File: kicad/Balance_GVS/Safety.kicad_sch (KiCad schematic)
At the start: 19 parts, among them K1 AQY210S, Q1 NPN, Q2 NPN, SW1 SW_Push, U4 INA303A1IPW, U6 OPA313IDCKR

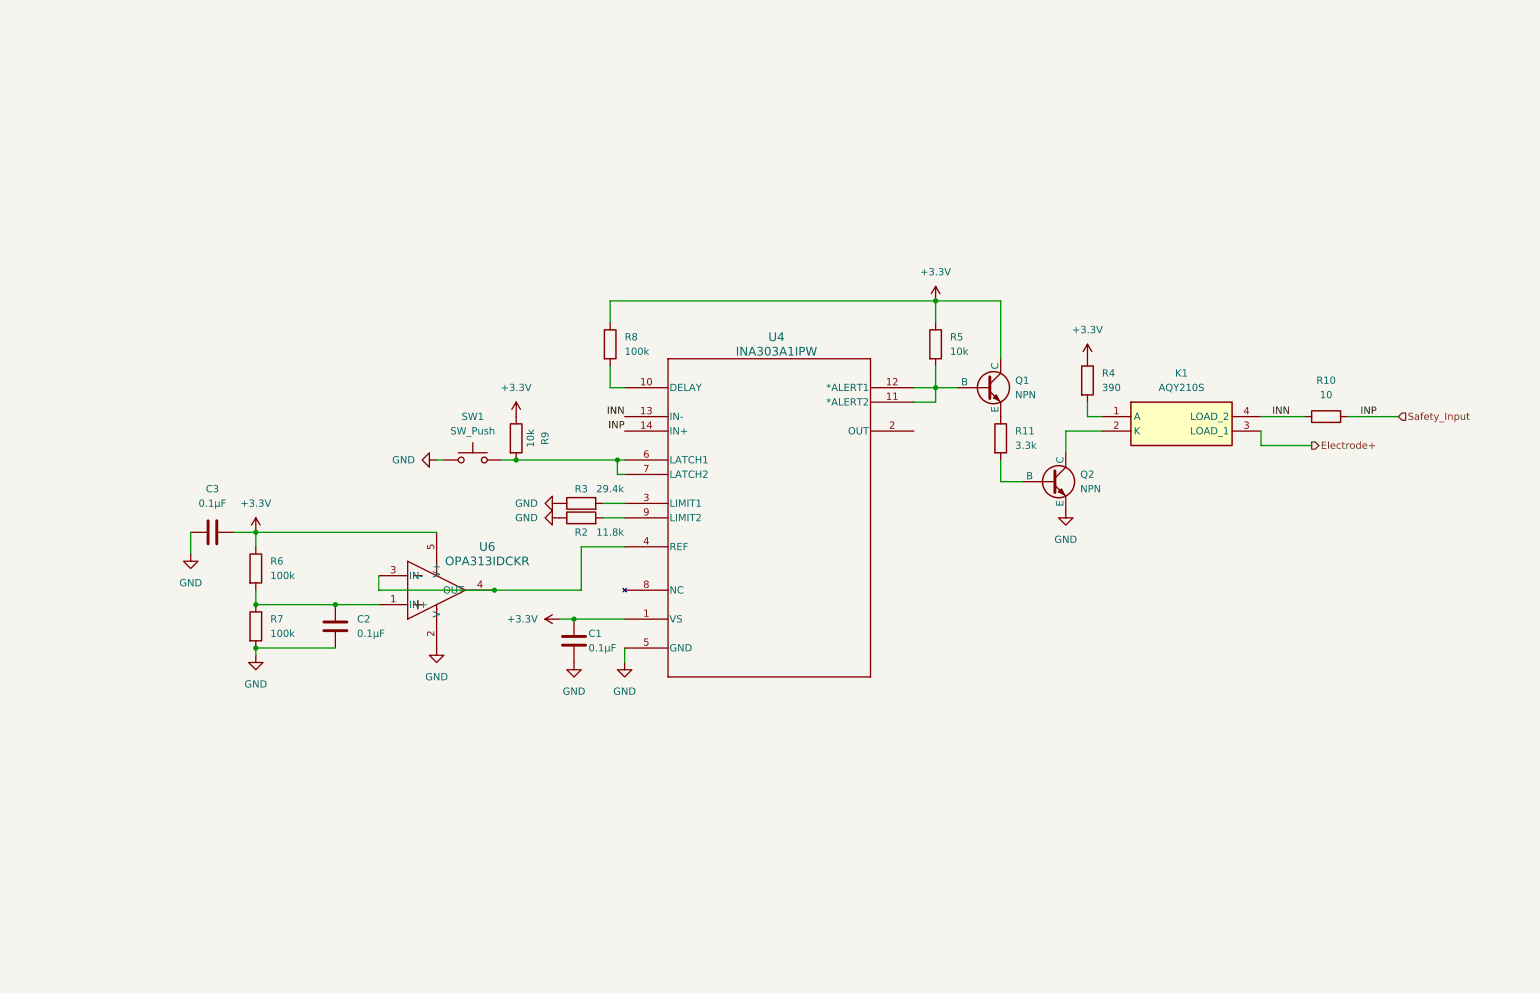
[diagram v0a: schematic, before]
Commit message: Update safety schematic with new limit set method
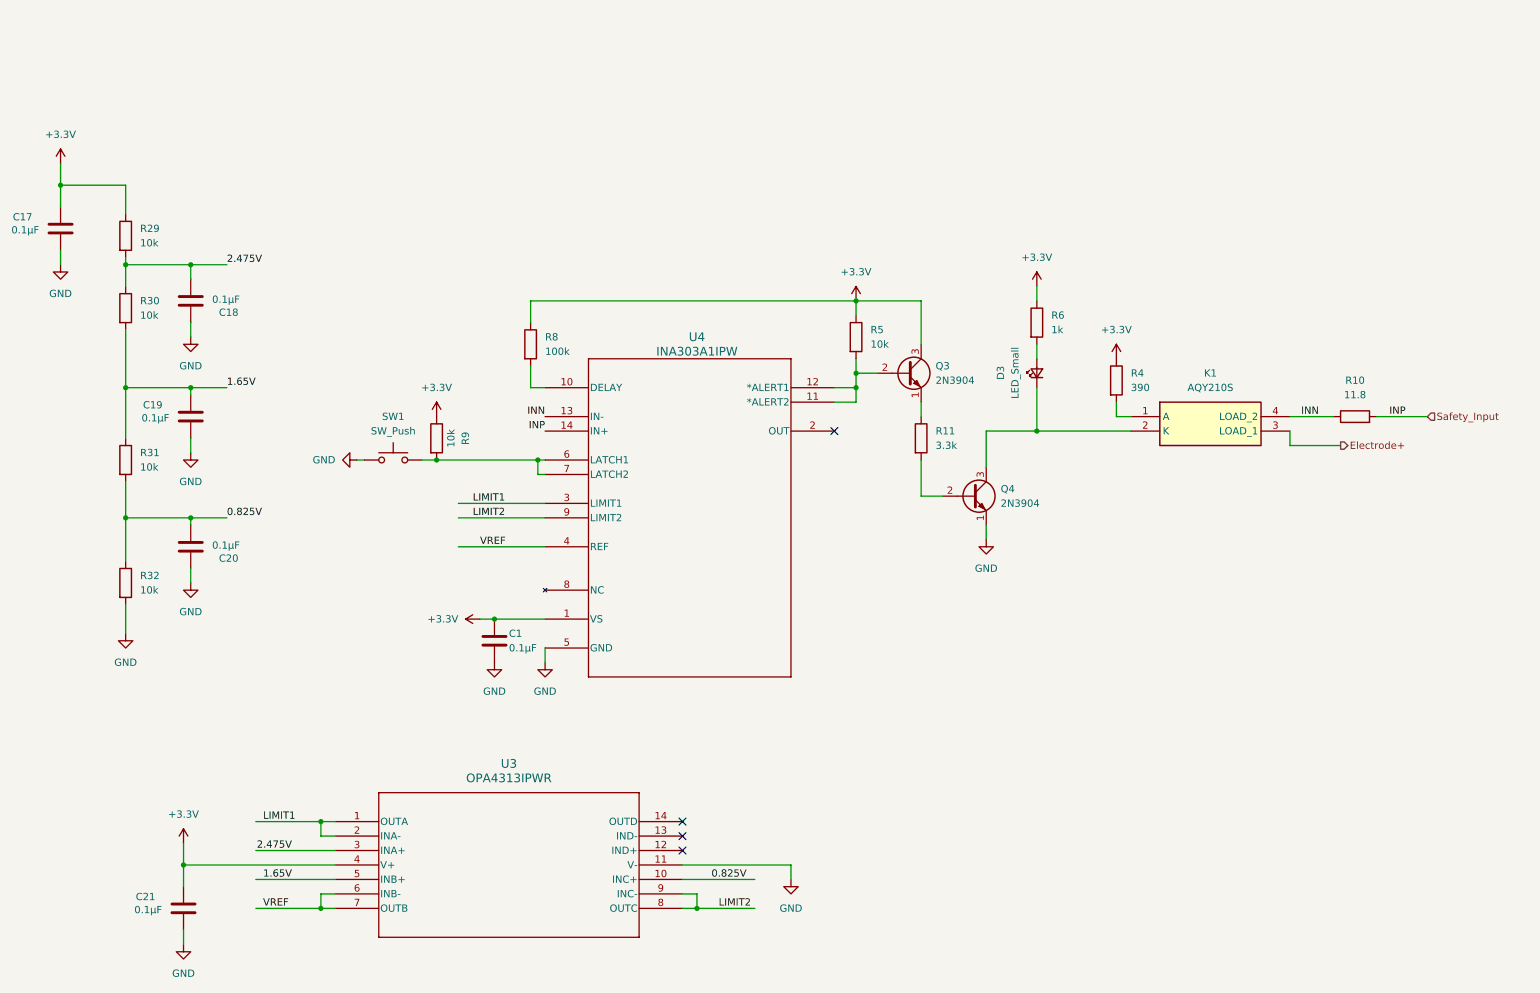
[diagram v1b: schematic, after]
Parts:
- removed C2, C3: 0.1µF, symbol Device:C
- removed Q1, Q2: NPN, symbol Simulation_SPICE:NPN
- removed R2: 11.8k, symbol Device:R
- removed R3: 29.4k, symbol Device:R
- removed R7: 100k, symbol Device:R
- removed U6: OPA313IDCKR, OPA313IDCKR_footprints:DCK0005A_N, symbol OPA313IDCKR:OPA313IDCKR
- added C17, C18, C19, C20, C21: 0.1µF, symbol Device:C
- added D3: LED_Small, symbol Device:LED_Small
- added Q3, Q4: 2N3904, Package_TO_SOT_THT:TO-92_Inline, symbol Transistor_BJT:2N3904
- added R29, R30, R31, R32: 10k, symbol Device:R
- added U3: OPA4313IPWR, PW14_TEX, symbol OPA4313IPWR:OPA4313IPWR
- R10: value 10 -> 11.8
- R6: value 100k -> 1k
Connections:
- net +3.3V: now also C17.1, C21.1, Q3.3 (C), R29.1, U3.4 (V+)
- net GND: now also C17.2, C18.1, C19.2, C20.1, C21.2, Q4.1 (E), R32.2, U3.11 (V-)
- net LIMIT1: now reaches U4.3 (LIMIT1)
- net LIMIT1: now also U3.1 (OUTA), U3.2 (INA-)
- net at R5.2, U4.11 (*ALERT2), U4.12 (*ALERT1): now also Q3.2 (B)
- net at R11.1: now also Q3.1 (E)
- net at K1.2 (K): now also D3.1 (K), Q4.3 (C)
- net LIMIT2: now reaches U4.9 (LIMIT2)
- net LIMIT2: now also U3.8 (OUTC), U3.9 (INC-)
- net at R6.2: now also D3.2 (A)
- net VREF: now reaches U4.4 (REF)
- net VREF: now also U3.6 (INB-), U3.7 (OUTB)
- net at R11.2: now also Q4.2 (B)
- new net 0.825V: C20.2, R31.2, R32.1, U3.10 (INC+)
- new net 1.65V: C19.1, R30.2, R31.1, U3.5 (INB+)
- new net 2.475V: C18.2, R29.2, R30.1, U3.3 (INA+)
- no-connect marks 0 -> 4
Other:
- moved on the sheet: C1, K1, R10, R11, R4, R5, R8, R9, SW1, U4

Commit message: Started adding howland connections
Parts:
- U3: footprint PW14_TEX -> OPA4313IPWR_footprints:PW14_TEX
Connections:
- net Electrode+ is gone; now on net INN: K1.3 (LOAD_1)
- net INN: no longer K1.4 (LOAD_2)
- net Safety_Input renamed Safety-
- new net Safety+: K1.4 (LOAD_2)
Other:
- moved on the sheet: R10
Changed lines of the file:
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@@
 	(wire
 		(pts
-			(xy 237.49 86.36) (xy 245.11 86.36)
+			(xy 248.92 86.36) (xy 248.92 85.09)
+		)
+		(stroke
+			(width 0)
+			(type default)
+		)
+	)
+	(wire
+		(pts
+			(xy 238.76 90.17) (xy 246.38 90.17)
 		)
 		(stroke
@@
 	(wire
 		(pts
+			(xy 237.49 86.36) (xy 248.92 86.36)
+		)
+		(stroke
+			(width 0)
+			(type default)
+		)
+	)
+	(wire
+		(pts
 			(xy 193.04 88.9) (xy 209.55 88.9)
 		)
@@
 	(wire
 		(pts
+			(xy 237.49 88.9) (xy 238.76 88.9)
+		)
+		(stroke
+			(width 0)
+			(type default)
+		)
+	)
+	(wire
+		(pts
 			(xy 106.68 129.54) (xy 106.68 127)
 		)
@@
 	(wire
 		(pts
-			(xy 252.73 86.36) (xy 261.62 86.36)
+			(xy 254 90.17) (xy 262.89 90.17)
 		)
 		(stroke
@@
 	(wire
 		(pts
-			(xy 55.88 162.56) (xy 69.85 162.56)
+			(xy 238.76 88.9) (xy 238.76 90.17)
 		)
 		(stroke
@@
 	(wire
 		(pts
-			(xy 104.14 66.04) (xy 161.29 66.04)
+			(xy 55.88 162.56) (xy 69.85 162.56)
 		)
 		(stroke
@@
 	(wire
 		(pts
-			(xy 184.15 88.9) (xy 193.04 88.9)
+			(xy 104.14 66.04) (xy 161.29 66.04)
 		)
 		(stroke
@@
 	(wire
 		(pts
-			(xy 44.45 59.69) (xy 50.8 59.69)
+			(xy 184.15 88.9) (xy 193.04 88.9)
 		)
 		(stroke
@@
 	(wire
 		(pts
-			(xy 172.72 66.04) (xy 172.72 73.66)
+			(xy 44.45 59.69) (xy 50.8 59.69)
 		)
 		(stroke
@@
 	(wire
 		(pts
-			(xy 85.09 93.98) (xy 87.63 93.98)
+			(xy 172.72 66.04) (xy 172.72 73.66)
 		)
 		(stroke
@@
 	(wire
 		(pts
-			(xy 33.02 59.69) (xy 44.45 59.69)
+			(xy 85.09 93.98) (xy 87.63 93.98)
 		)
 		(stroke
@@
 	(wire
 		(pts
-			(xy 33.02 97.79) (xy 33.02 111.76)
+			(xy 33.02 59.69) (xy 44.45 59.69)
 		)
 		(stroke
@@
 	(wire
 		(pts
-			(xy 237.49 88.9) (xy 237.49 91.44)
+			(xy 33.02 97.79) (xy 33.02 111.76)
 		)
 		(stroke
@@
 	(wire
 		(pts
-			(xy 237.49 91.44) (xy 246.38 91.44)
-		)
-		(stroke
-			(width 0)
-			(type default)
-		)
-	)
-	(wire
-		(pts
 			(xy 207.01 86.36) (xy 207.01 83.82)
 		)
@@
 	)
 	(label "INP"
-		(at 257.81 86.36 180)
+		(at 259.08 90.17 180)
 		(effects
 			(font
@@
 		)
 	)
-	(label "1.65V"
-		(at 62.23 167.64 180)
-		(effects
-			(font
-				(size 1.27 1.27)
-			)
-			(justify right bottom)
-		)
-	)
 	(label "LIMIT2"
 		(at 137.16 172.72 0)
@@
 	)
 	(label "INN"
-		(at 242.57 86.36 180)
+		(at 243.84 90.17 180)
 		(effects
 			(font
@@
 		)
 	)
-	(label "1.65V"
-		(at 50.8 81.28 0)
+	(global_label "1.65V"
+		(shape input)
+		(at 55.88 167.64 180)
+		(fields_autoplaced yes)
 		(effects
 			(font
 				(size 1.27 1.27)
 			)
-			(justify left bottom)
+			(justify right)
+		)
+		(property "Intersheetrefs" "${INTERSHEET_REFS}"
+			(at 47.5729 167.64 0)
+			(hide yes)
+			(show_name no)
+			(do_not_autoplace no)
+			(effects
+				(font
+					(size 1.27 1.27)
+				)
+				(justify right)
+			)
 		)
 	)
-	(hierarchical_label "Electrode+"
-		(shape output)
-		(at 246.38 91.44 0)
+	(global_label "Safety-"
+		(shape bidirectional)
+		(at 262.89 90.17 0)
+		(fields_autoplaced yes)
 		(effects
 			(font
@@
 			(justify left)
 		)
+		(property "Intersheetrefs" "${INTERSHEET_REFS}"
+			(at 274.425 90.17 0)
+			(hide yes)
+			(show_name no)
+			(do_not_autoplace no)
+			(effects
+				(font
+					(size 1.27 1.27)
+				)
+				(justify left)
+			)
+		)
 	)
-	(hierarchical_label "Safety_Input"
-		(shape input)
-		(at 261.62 86.36 0)
+	(global_label "Safety+"
+		(shape bidirectional)
+		(at 248.92 85.09 0)
+		(fields_autoplaced yes)
 		(effects
 			(font
@@
 			(justify left)
 		)
+		(property "Intersheetrefs" "${INTERSHEET_REFS}"
+			(at 260.455 85.09 0)
+			(hide yes)
+			(show_name no)
+			(do_not_autoplace no)
+			(effects
+				(font
+					(size 1.27 1.27)
+				)
+				(justify left)
+			)
+		)
+	)
+	(global_label "1.65V"
+		(shape output)
+		(at 50.8 81.28 0)
+		(fields_autoplaced yes)
+		(effects
+			(font
+				(size 1.27 1.27)
+			)
+			(justify left)
+		)
+		(property "Intersheetrefs" "${INTERSHEET_REFS}"
+			(at 59.1071 81.28 0)
+			(hide yes)
+			(show_name no)
+			(do_not_autoplace no)
+			(effects
+				(font
+					(size 1.27 1.27)
+				)
+				(justify left)
+			)
+		)
 	)
 	(symbol
@@
 	(symbol
 		(lib_id "Device:R")
-		(at 248.92 86.36 90)
+		(at 250.19 90.17 90)
 		(unit 1)
 		(body_style 1)
@@
 		(in_pos_files yes)
 		(dnp no)
-		(fields_autoplaced yes)
 		(property "Reference" "R10"
-			(at 248.92 80.01 90)
+			(at 250.19 93.472 90)
 			(show_name no)
 			(do_not_autoplace no)
@@
 		)
 		(property "Value" "11.8"
-			(at 248.92 82.55 90)
+			(at 250.19 96.012 90)
 			(show_name no)
 			(do_not_autoplace no)
@@
 		)
 		(property "Footprint" ""
-			(at 248.92 88.138 90)
+			(at 250.19 91.948 90)
 			(hide yes)
 			(show_name no)
@@
 		)
 		(property "Datasheet" ""
-			(at 248.92 86.36 0)
+			(at 250.19 90.17 0)
 			(hide yes)
 			(show_name no)
@@
 		)
 		(property "Description" ""
-			(at 248.92 86.36 0)
+			(at 250.19 90.17 0)
 			(show_name no)
 			(do_not_autoplace no)
@@
 			)
 		)
-		(property "Footprint" "PW14_TEX"
+		(property "Footprint" "OPA4313IPWR_footprints:PW14_TEX"
 			(at 69.85 157.48 0)
 			(hide yes)

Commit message: Finish Howland
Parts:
- added J1: Conn_01x02_Pin, Package_CSP:Xilinx_CSG48_7.0x7.0mm_Layout7x7_P0.8mm, symbol Connector:Conn_01x02_Pin
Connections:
- net Safety-: now also U4.13 (IN-); no longer U4.14 (IN+)
- net INN renamed INP
- net INP: now also U4.14 (IN+); no longer U4.13 (IN-)
- net Safety+ renamed Electrode-
- net Electrode-: now also J1.1 (Pin_1)
- new net Electrode+: J1.2 (Pin_2)
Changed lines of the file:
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@@
+	(wire
+		(pts
+			(xy 250.19 72.39) (xy 247.65 72.39)
+		)
+		(stroke
+			(width 0)
+			(type default)
+		)
+	)
 	(wire
 		(pts
@@
 	(wire
 		(pts
-			(xy 248.92 86.36) (xy 248.92 85.09)
-		)
-		(stroke
-			(width 0)
-			(type default)
-		)
-	)
-	(wire
-		(pts
 			(xy 238.76 90.17) (xy 246.38 90.17)
 		)
@@
 	(wire
 		(pts
+			(xy 237.49 85.09) (xy 237.49 86.36)
+		)
+		(stroke
+			(width 0)
+			(type default)
+		)
+	)
+	(wire
+		(pts
 			(xy 55.88 157.48) (xy 67.31 157.48)
 		)
@@
 	(wire
 		(pts
-			(xy 237.49 86.36) (xy 248.92 86.36)
+			(xy 237.49 85.09) (xy 248.92 85.09)
 		)
 		(stroke
@@
 	(wire
 		(pts
+			(xy 250.19 64.77) (xy 250.19 67.31)
+		)
+		(stroke
+			(width 0)
+			(type default)
+		)
+	)
+	(wire
+		(pts
 			(xy 21.59 45.72) (xy 33.02 45.72)
 		)
@@
 	(wire
 		(pts
+			(xy 250.19 67.31) (xy 254 67.31)
+		)
+		(stroke
+			(width 0)
+			(type default)
+		)
+	)
+	(wire
+		(pts
 			(xy 130.81 172.72) (xy 133.35 172.72)
 		)
@@
 	(wire
 		(pts
+			(xy 250.19 69.85) (xy 250.19 72.39)
+		)
+		(stroke
+			(width 0)
+			(type default)
+		)
+	)
+	(wire
+		(pts
 			(xy 67.31 157.48) (xy 67.31 160.02)
 		)
@@
 	(wire
 		(pts
+			(xy 247.65 64.77) (xy 250.19 64.77)
+		)
+		(stroke
+			(width 0)
+			(type default)
+		)
+	)
+	(wire
+		(pts
 			(xy 238.76 88.9) (xy 238.76 90.17)
+		)
+		(stroke
+			(width 0)
+			(type default)
+		)
+	)
+	(wire
+		(pts
+			(xy 254 69.85) (xy 250.19 69.85)
 		)
 		(stroke
@@
 		)
 	)
-	(label "INP"
+	(label "INN"
 		(at 259.08 90.17 180)
 		(effects
@@
 		)
 	)
-	(label "INN"
+	(label "INP"
 		(at 243.84 90.17 180)
 		(effects
@@
 		)
 	)
-	(global_label "Safety+"
+	(global_label "Electrode-"
+		(shape input)
+		(at 247.65 72.39 180)
+		(fields_autoplaced yes)
+		(effects
+			(font
+				(size 1.27 1.27)
+			)
+			(justify right)
+		)
+		(property "Intersheetrefs" "${INTERSHEET_REFS}"
+			(at 234.2025 72.39 0)
+			(hide yes)
+			(show_name no)
+			(do_not_autoplace no)
+			(effects
+				(font
+					(size 1.27 1.27)
+				)
+				(justify right)
+			)
+		)
+	)
+	(global_label "Electrode-"
 		(shape bidirectional)
 		(at 248.92 85.09 0)
@@
 		)
 		(property "Intersheetrefs" "${INTERSHEET_REFS}"
-			(at 260.455 85.09 0)
+			(at 263.4788 85.09 0)
 			(hide yes)
 			(show_name no)
@@
 				)
 				(justify left)
+			)
+		)
+	)
+	(global_label "Electrode+"
+		(shape input)
+		(at 247.65 64.77 180)
+		(fields_autoplaced yes)
+		(effects
+			(font
+				(size 1.27 1.27)
+			)
+			(justify right)
+		)
+		(property "Intersheetrefs" "${INTERSHEET_REFS}"
+			(at 234.2025 64.77 0)
+			(hide yes)
+			(show_name no)
+			(do_not_autoplace no)
+			(effects
+				(font
+					(size 1.27 1.27)
+				)
+				(justify right)
 			)
 		)
@@
 					(unit 1)
 				)
+			)
+		)
+	)
+	(symbol
+		(lib_id "Connector:Conn_01x02_Pin")
+		(at 259.08 69.85 180)
+		(unit 1)
+		(body_style 1)
+		(exclude_from_sim no)
+		(in_bom yes)
+		(on_board yes)
+		(in_pos_files yes)
+		(dnp no)
+		(fields_autoplaced yes)
+		(property "Reference" "J1"
+			(at 260.35 67.3099 0)
+			(show_name no)
+			(do_not_autoplace no)
+			(effects
+				(font
+					(size 1.27 1.27)
+				)
+				(justify right)
+			)
+		)
+		(property "Value" "Conn_01x02_Pin"
+			(at 260.35 69.8499 0)
+			(show_name no)
+			(do_not_autoplace no)
+			(effects
+				(font
+					(size 1.27 1.27)
+				)
+				(justify right)
+			)
+		)
+		(property "Footprint" "Package_CSP:Xilinx_CSG48_7.0x7.0mm_Layout7x7_P0.8mm"
+			(at 259.08 69.85 0)
+			(hide yes)
+			(show_name no)
+			(do_not_autoplace no)
+			(effects
+				(font
+					(size 1.27 1.27)
+				)
+			)
+		)
+		(property "Datasheet" ""
+			(at 259.08 69.85 0)
+			(hide yes)
+			(show_name no)
+			(do_not_autoplace no)
+			(effects
+				(font
+					(size 1.27 1.27)
+				)
+			)
+		)
+		(property "Description" "Generic connector, single row, 01x02, script generated"
+			(at 259.08 69.85 0)
+			(hide yes)
+			(show_name no)
+			(do_not_autoplace no)
+			(effects
+				(font
+					(size 1.27 1.27)
+				)
+			)
+		)
+		(pin "1"
+		)
+		(pin "2"
+		)
+		(instances
+			(project "Balance_GVS"
+				(path "/fe65ed2a-e0ad-4542-81bb-0c202b789e4d/317fc989-07fa-4225-9b72-e0cc907dbbff"
+					(reference "J1")
+					(unit 1)
+				)

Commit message: Add Processor User IO
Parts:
- R6: value 1k -> 300
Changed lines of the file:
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@@
 			)
 		)
-		(property "Value" "1k"
+		(property "Value" "300"
 			(at 195.58 71.12 0)
 			(show_name no)

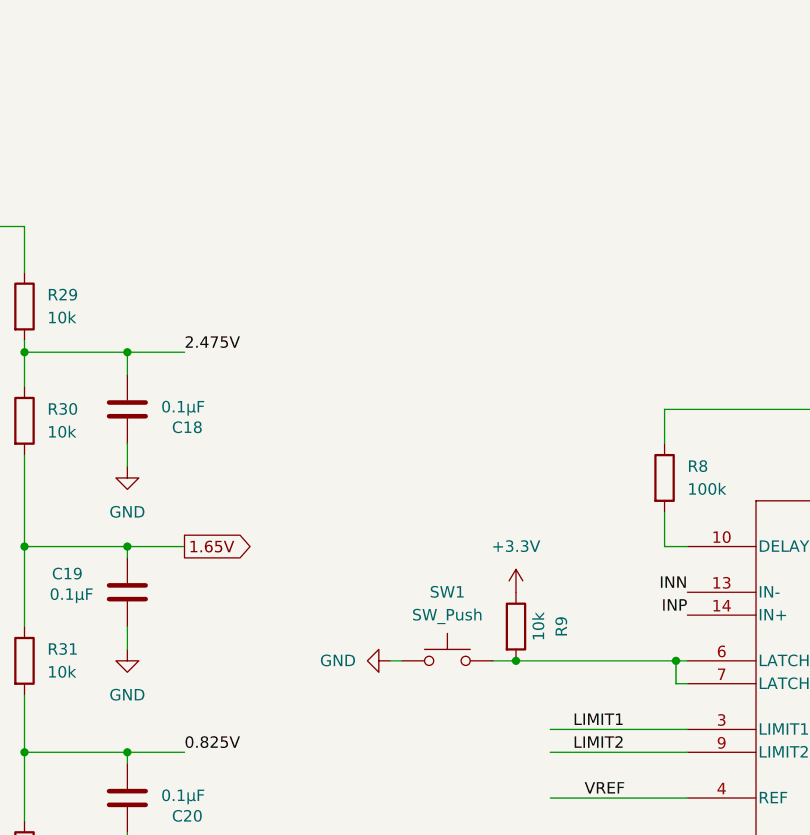
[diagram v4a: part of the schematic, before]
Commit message: Add Footprints to Schematic
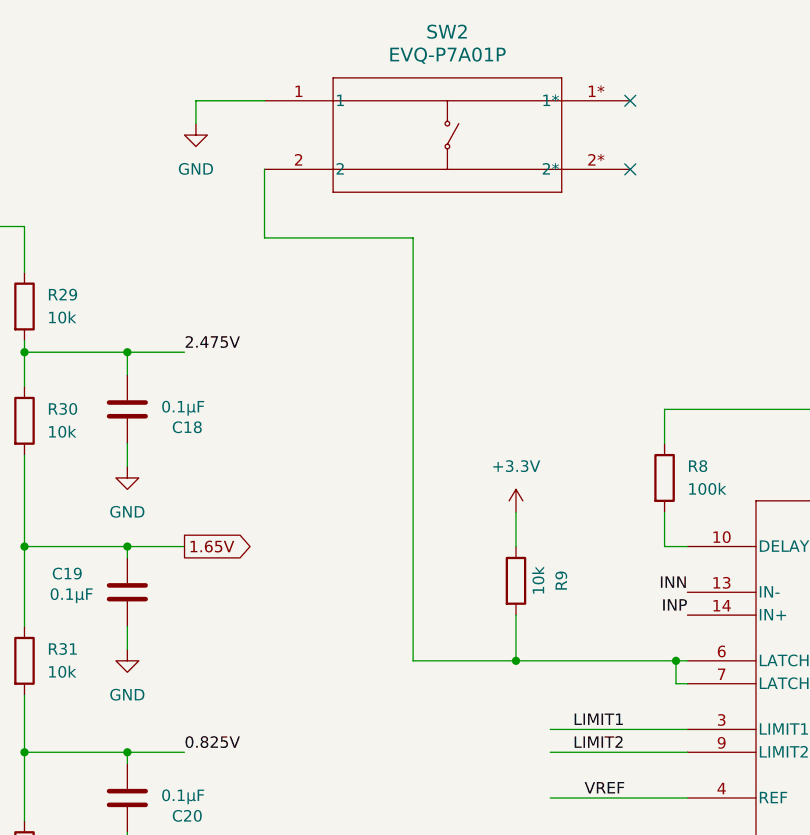
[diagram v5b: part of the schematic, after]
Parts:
- removed SW1: SW_Push, symbol Switch:SW_Push
- added SW2: EVQ-P7A01P, EVQ_P7A01P:EVQ_P7_PAN, symbol EVQ_P7A01P:EVQ-P7A01P
- C1, C17, C18, C19, C20, C21: footprint (none) -> Capacitor_SMD:C_0805_2012Metric_Pad1.18x1.45mm_HandSolder
- D3: footprint (none) -> LED_SMD:LED_0603_1608Metric_Pad1.05x0.95mm_HandSolder
- J1: footprint Package_CSP:Xilinx_CSG48_7.0x7.0mm_Layout7x7_P0.8mm -> Connector_PinSocket_2.54mm:PinSocket_1x02_P2.54mm_Vertical
- R10, R11, R29, R30, R31, R32, R4, R5, R6, R8, R9: footprint (none) -> Resistor_SMD:R_0805_2012Metric_Pad1.20x1.40mm_HandSolder
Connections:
- net GND: now also SW2.1
- net at R9.2, U4.6 (LATCH1), U4.7 (LATCH2): now also SW2.2
- no-connect marks 4 -> 6
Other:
- moved on the sheet: R9

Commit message: Add shit ton to schematic
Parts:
- added D10, D11, D12, D4: BAS40, BAS40:P200_SOT-23, symbol BAS40:Diode-NC_pin
- added D13: CMJ3500, Diode_SMD:D_SOD-123F, symbol Device:D_45deg
- added D14, D15: CMJ3500, Diode_SMD:D_SOD-123F, symbol Device:D
- added J6, J7: Conn_01x03_Pin, Connector_PinHeader_2.54mm:PinHeader_1x03_P2.54mm_Vertical, symbol Connector:Conn_01x03_Pin
- added J8: Conn_01x05_Pin, Connector_PinSocket_2.54mm:PinSocket_1x05_P2.54mm_Vertical, symbol Connector:Conn_01x05_Pin
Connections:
- net Electrode+: now also J8.1 (Pin_1)
- net Electrode-: now also J6.2 (Pin_2), J8.2 (Pin_2); no longer K1.4 (LOAD_2)
- net Safety-: now also J8.4 (Pin_4)
- new net: D11.1 (A), D12.1 (A), D13.1 (K)
- new net: D10.1 (A), D12.2 (C), J7.1 (Pin_1)
- new net: D10.2 (C), D13.2 (A), D4.2 (C)
- new net: D14.1 (K), D15.1 (K)
- new net: D15.2 (A), J7.3 (Pin_3)
- new net: D14.2 (A), J6.1 (Pin_1)
- new net: D11.2 (C), D4.1 (A), J6.3 (Pin_3)
- new net Current_Sense-: J8.5 (Pin_5)
- new net Safety+: J7.2 (Pin_2), J8.3 (Pin_3), K1.4 (LOAD_2)
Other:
- moved on the sheet: D3, J1, K1, Q4, R10, R4, R6
